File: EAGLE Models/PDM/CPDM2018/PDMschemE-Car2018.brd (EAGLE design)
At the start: 85.1 x 102.9 mm, 45 parts, among them Q1 2N2907, Q2 2N2907, Q3 2N2907, Q4 2N2907, Q5 2N2907, Q6 2N2907

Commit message: added connector to daughter card, moved connector on pdm
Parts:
- moved U$2 63.8 mm to (24.1, 39.4), turned to 180 degrees
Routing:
- net DC/BSPD: track 30.5 -> 51.6 mm
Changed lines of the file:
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@@
 <?xml version="1.0" encoding="utf-8"?>
 <!DOCTYPE eagle SYSTEM "eagle.dtd">
-<eagle version="8.3.2">
+<eagle version="8.4.0">
 <drawing>
 <settings>
@@
 <param name="dpMaxLengthDifference" value="10mm"/>
 <param name="dpGapFactor" value="2.5"/>
-<param name="checkGrid" value="0"/>
-<param name="checkAngle" value="0"/>
 <param name="checkFont" value="1"/>
 <param name="checkRestrict" value="1"/>
+<param name="checkStop" value="0"/>
 <param name="useDiameter" value="13"/>
 <param name="maxErrors" value="50"/>
@@
 <element name="R9" library="resistor" library_urn="urn:adsk.eagle:library:348" package="R1206" package3d_urn="urn:adsk.eagle:package:26062/1" value="470" x="27.94" y="58.42" rot="R90"/>
 <element name="U$1" library="infineon" package="TO220-3" value="IRF40B207" x="39.37" y="96.52" rot="R270"/>
-<element name="U$2" library="formula electric" package="HARWIN_M20-9980445" value="HARWIN_M20-9980445" x="57.15" y="93.98" locked="yes" rot="R270"/>
+<element name="U$2" library="formula electric" package="HARWIN_M20-9980445" value="HARWIN_M20-9980445" x="24.13" y="39.37" locked="yes" rot="R180"/>
 <element name="U$5" library="diodes-inc" package="SOT23-3" value="MMBD4448H-7-F" x="2.54" y="39.37" rot="R270"/>
 <element name="U$7" library="diodes-inc" package="SOT23-3" value="MMBD4448H-7-F" x="2.54" y="35.56" rot="R270"/>
@@
 <contactref element="W.PUMPRELAY" pad="COIL1"/>
 <contactref element="U$2" pad="P1"/>
-<wire x1="3.64" y1="39.37" x2="58.42" y2="97.79" width="0" layer="19" extent="1-1"/>
+<wire x1="3.64" y1="39.37" x2="27.94" y2="38.1" width="0" layer="19" extent="1-1"/>
 <wire x1="3.3782" y1="22.0218" x2="3.64" y2="39.37" width="0" layer="19" extent="1-1"/>
 </signal>
@@
 <contactref element="FANRELAY" pad="COIL1"/>
 <contactref element="U$2" pad="P5"/>
-<wire x1="3.64" y1="35.56" x2="55.88" y2="97.79" width="0" layer="19" extent="1-1"/>
+<wire x1="3.64" y1="35.56" x2="27.94" y2="40.64" width="0" layer="19" extent="1-1"/>
 <wire x1="3.3782" y1="30.9118" x2="3.64" y2="35.56" width="0" layer="19" extent="1-1"/>
 </signal>
@@
 <contactref element="U$6" pad="P$2"/>
 <contactref element="U$6" pad="P$3"/>
-<wire x1="55.88" y1="92.71" x2="58.42" y2="92.71" width="0" layer="19" extent="1-1"/>
-<wire x1="50.8" y1="91.592" x2="55.88" y2="92.71" width="0" layer="19" extent="1-1"/>
+<wire x1="22.86" y1="40.64" x2="22.86" y2="38.1" width="0" layer="19" extent="1-1"/>
+<wire x1="50.8" y1="91.592" x2="22.86" y2="40.64" width="0" layer="19" extent="1-1"/>
 <wire x1="46.99" y1="91.592" x2="50.8" y2="91.592" width="0" layer="19" extent="1-1"/>
 <wire x1="39.37" y1="93.98" x2="46.99" y2="91.592" width="0" layer="19" extent="1-1"/>
@@
 <contactref element="U$1" pad="G"/>
 <contactref element="U$2" pad="P6"/>
-<wire x1="39.37" y1="99.06" x2="55.88" y2="95.25" width="0" layer="19" extent="1-1"/>
+<wire x1="39.37" y1="99.06" x2="25.4" y2="40.64" width="0" layer="19" extent="1-1"/>
 <wire x1="33.172" y1="97.79" x2="39.37" y2="99.06" width="0" layer="19" extent="1-1"/>
 </signal>
@@
 <contactref element="U$2" pad="P8"/>
 <contactref element="U$2" pad="P4"/>
-<wire x1="55.88" y1="90.17" x2="58.42" y2="90.17" width="0" layer="19" extent="1-1"/>
-<wire x1="57.9882" y1="64.643" x2="58.42" y2="90.17" width="0" layer="19" extent="1-1"/>
+<wire x1="20.32" y1="40.64" x2="20.32" y2="38.1" width="0" layer="19" extent="1-1"/>
+<wire x1="57.9882" y1="64.643" x2="20.32" y2="38.1" width="0" layer="19" extent="1-1"/>
 <wire x1="61.3918" y1="64.643" x2="57.9882" y2="64.643" width="0" layer="19" extent="1-1"/>
 <wire x1="32.33" y1="73.66" x2="57.9882" y2="64.643" width="0" layer="19" extent="16-16"/>
 <wire x1="58.42" y1="64.77" x2="60.96" y2="64.77" width="1.27" layer="1"/>
-<wire x1="58.42" y1="64.77" x2="58.42" y2="90.17" width="1.27" layer="1"/>
-<wire x1="58.42" y1="90.17" x2="55.88" y2="90.17" width="1.27" layer="1"/>
+<wire x1="58.42" y1="64.77" x2="20.32" y2="38.1" width="1.27" layer="1"/>
+<wire x1="20.32" y1="38.1" x2="20.32" y2="40.64" width="1.27" layer="1"/>
 </signal>
 <signal name="FRONT/REAR_HARNESS">

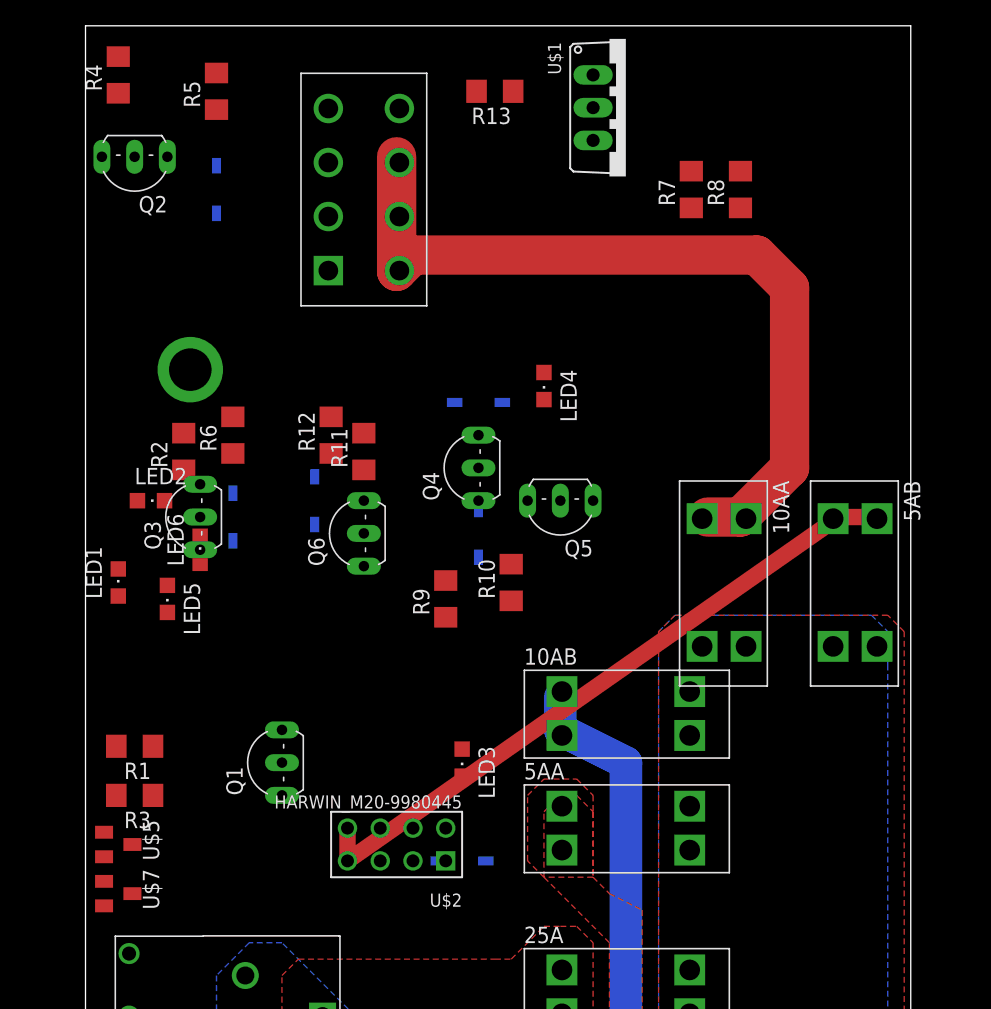
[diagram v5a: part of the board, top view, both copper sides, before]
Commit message: Arranged component groups
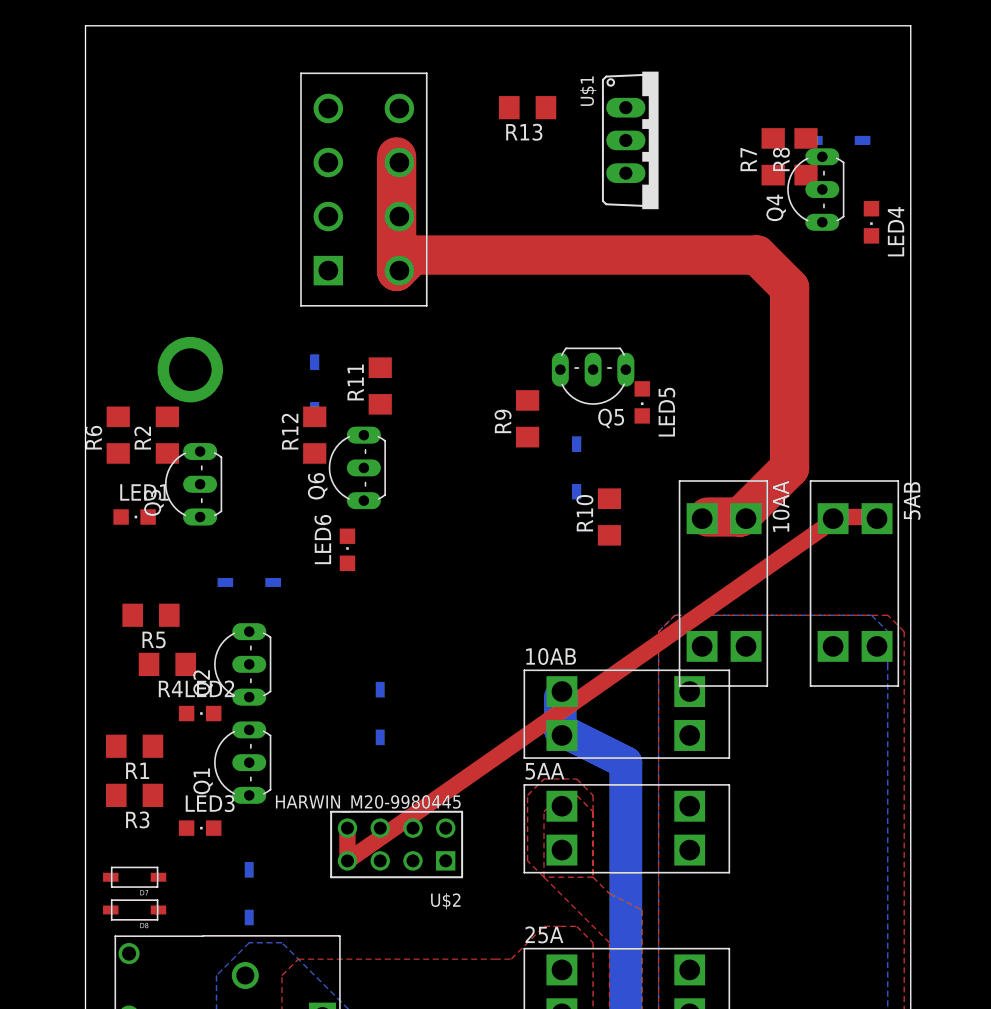
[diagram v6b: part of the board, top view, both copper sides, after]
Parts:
- removed U$5, U$7: MMBD4448H-7-F, diodes-inc:SOT23-3
- added D7, D8: (no value), adafruit:SOD-123
- moved R4 45.9 mm to (6.35, 53.3), turned to 180 degrees
- moved D2 42.6 mm to (22.9, 49.5)
- moved R5 41.0 mm to (5.08, 57.1), turned to 180 degrees
- moved LED5 39.9 mm to (43.2, 73.7)
- moved Q2 38.9 mm to (11.4, 53.3), turned to 90 degrees
- moved D4 34.5 mm to (58.4, 94.0)
- moved Q4 34.3 mm to (55.9, 90.2)
- moved LED4 28.4 mm to (61.0, 87.6)
- moved LED3 20.9 mm to (8.89, 40.6), turned to 270 degrees
- moved LED2 16.9 mm to (8.89, 49.5)
- moved D1 16.7 mm to (12.7, 35.6), turned to 270 degrees
- moved R9 15.3 mm to (34.3, 72.4)
- moved LED6 11.4 mm to (20.3, 62.2)
- moved Q5 10.5 mm to (39.4, 74.9)
- moved D5 9.16 mm to (38.1, 68.6)
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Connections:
- net F.RELAY: now also D7.C; no longer U$7.3
- net GND: now also D7.A, D8.A; no longer U$5.1, U$7.1
- net P.RELAY: now also D8.C; no longer U$5.3

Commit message: PDM Completed Rev1
All components have traces; waiting for feedback
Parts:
- D7: value (none) -> 1N4148
- moved U$1 61.9 mm to (25.4, 34.3), turned to 180 degrees
- moved LED4 59.8 mm to (2.54, 74.9)
- moved R13 57.2 mm to (31.8, 39.4), flipped to the bottom, turned to 90 degrees
- moved R8 51.0 mm to (7.62, 76.2), flipped to the bottom, turned to 0 degrees
- moved R7 47.5 mm to (7.62, 80.0), flipped to the bottom, turned to 0 degrees
- moved Q4 45.4 mm to (12.7, 76.2)
- moved D4 44.4 mm to (20.3, 71.1), turned to 270 degrees
- moved LED6 36.6 mm to (40.6, 92.7), turned to 90 degrees
- moved R12 29.2 mm to (41.9, 87.6), flipped to the bottom
- moved D6 26.7 mm to (44.5, 74.9), turned to 180 degrees
- moved R11 26.2 mm to (45.7, 87.6), flipped to the bottom
- moved Q6 25.7 mm to (41.9, 82.5), turned to 0 degrees
- moved R9 25.4 mm to (54.6, 87.6), flipped to the bottom
- moved R10 25.0 mm to (50.8, 87.6), flipped to the bottom
- moved 5AB 21.8 mm to (41.9, 47.0), turned to 0 degrees
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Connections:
- net DC/BSPD: now also U$2.P1, U$2.P5; no longer U$2.P4, U$2.P8
- net F.RELAY: now also U$2.P8; no longer U$2.P5
- net P.RELAY: now also U$2.P4; no longer U$2.P1
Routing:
- net GND: track 0.00 -> 274.2 mm, vias 0 -> 1
- net MCU_POWER: track 0.00 -> 173.4 mm
- net 12V: track 0.00 -> 141.3 mm
- net FRONT/REAR_HARNESS: track 48.6 -> 151.2 mm
- net FAN_PWM_OUT: track 0.00 -> 65.1 mm
- net BAT_BOX: track 0.00 -> 63.8 mm
- net SBRIO/BMS/WIFI: track 62.8 -> 92.2 mm
- net P.RELAY: track 0.00 -> 28.7 mm
- net F.RELAY: track 0.00 -> 25.2 mm
- net N$10: track 0.00 -> 22.2 mm
- net N$4: track 0.00 -> 21.0 mm
- net N$6: track 0.00 -> 14.6 mm
- net FAN_PWM_IN: track 0.00 -> 14.1 mm
- net N$18: track 0.00 -> 13.0 mm
- net N$17: track 0.00 -> 11.8 mm
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- removed copper zone on layer 1, net BAT_BOX
